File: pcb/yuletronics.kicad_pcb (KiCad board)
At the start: 2 copper layers, 45 x 50 mm, 35 parts, among them IC1 STM32F042F6P6, IC2 MCP1700, IC3 TLV61225, J1 BATT, J2 MICROUSB, P1 SWD_TC, SW1 BOOTLOAD, SW2 PWR_SWITCH

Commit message: Version 1
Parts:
- removed D1, D2, D4, D7, D8: LED, agg:0805-LED
- removed R10, R11, R5, R6, R8, R9: R, agg:0805
- added D10: LED_RABG, yule:CREE_RGB_LED, F.Cu at (95.8, 82.8)
- added D13: LED_RABG, yule:CREE_RGB_LED, F.Cu at (143.0, 102.9)
- added D14: LED_RABG, yule:CREE_RGB_LED, F.Cu at (131.8, 70.2)
- added J3: CONN_01x08, yule:Interboard, B.Cu at (117.0, 55.5)
- added R12: 510, agg:0805, F.Cu at (108.0, 70.0)
- added R15: 510, agg:0805, F.Cu at (108.0, 72.0)
- added R17: 510, agg:0805, F.Cu at (96.0, 101.0)
- added R18: 510, agg:0805, F.Cu at (132.0, 85.0)
- added R20: 510, agg:0805, F.Cu at (96.0, 103.0)
- added R21: 510, agg:0805, F.Cu at (132.0, 83.0)
- added R23: 510, agg:0805, F.Cu at (96.0, 105.0)
- added R24: 510, agg:0805, F.Cu at (132.0, 81.0)
- added R26: 510, agg:0805, F.Cu at (100.0, 81.0)
- added R29: 510, agg:0805, F.Cu at (100.0, 83.0)
- added R32: 510, agg:0805, F.Cu at (100.0, 85.0)
- added R35: 510, agg:0805, F.Cu at (138.0, 105.0)
- added R36: 510, agg:0805, F.Cu at (126.0, 72.0)
- added R38: 510, agg:0805, F.Cu at (138.0, 103.0)
- added R39: 510, agg:0805, F.Cu at (126.0, 70.0)
- added R41: 510, agg:0805, F.Cu at (138.0, 101.0)
- added R42: 510, agg:0805, F.Cu at (126.0, 68.0)
- added SW3: BUTTON, yule:MOM_SWITCH, B.Cu at (132.0, 94.9)
- added X1: Silk_art, yule:tree_silk_scaled, F.Cu at (117.0, 89.8)
- D3, D5, D6: value LED -> LED_RABG; footprint agg:0805-LED -> yule:CREE_RGB_LED
- R4: value R -> 10k
- R7: value R -> 510
- SW1: footprint agg:MOM_SWITCH -> yule:MOM_SWITCH; moved to B.Cu
- SW2: moved to B.Cu
- moved D5 55.7 mm to (91.2, 102.9), turned to 0 degrees
- moved SW1 33.2 mm to (102.0, 94.9), turned to 270 degrees
- moved C5 32.6 mm to (105.0, 119.6), turned to 180 degrees
- moved D3 32.2 mm to (102.2, 70.2), turned to 0 degrees
- moved R7 30.5 mm to (108.0, 68.0), turned to 0 degrees
- moved C6 30.0 mm to (105.0, 122.2), turned to 180 degrees
- moved IC2 27.1 mm to (109.0, 121.4), turned to 0 degrees
- moved L1 25.8 mm to (105.5, 114.7)
- moved C7 25.7 mm to (105.5, 109.4)
- moved C4 25.6 mm to (105.5, 117.5)
- moved IC3 25.5 mm to (105.5, 112.2)
- moved R4 25.0 mm to (138.0, 98.2), turned to 0 degrees
- moved SW2 24.7 mm to (105.4, 105.3), turned to 0 degrees
- moved R1 24.2 mm to (107.0, 97.2), turned to 90 degrees
- moved J1 13.9 mm to (117.0, 114.9), turned to 180 degrees
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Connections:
- D3 pad 1: GND -> Net-(D3-Pad1)
- D3 pad 2: Net-(D3-Pad2) -> 3v3
- D5 pad 1: GND -> Net-(D5-Pad1)
- D5 pad 2: Net-(D5-Pad2) -> 3v3
- D6 pad 1: GND -> Net-(D6-Pad1)
- D6 pad 2: Net-(D6-Pad2) -> 3v3
- IC1 pad 10: /LED5 -> /LED2G
- IC1 pad 12: /LED6 -> /LED2B
- IC1 pad 13: /LED7 -> /BUTTON
- IC1 pad 14: /LED8 -> (no net)
- IC1 pad 2: Net-(IC1-Pad2) -> (no net)
- IC1 pad 3: Net-(IC1-Pad3) -> (no net)
- IC1 pad 4: Net-(IC1-Pad4) -> (no net)
- IC1 pad 6: /LED1 -> /LED1R
- IC1 pad 7: /LED2 -> /LED1G
- IC1 pad 8: /LED3 -> /LED1B
- IC1 pad 9: /LED4 -> /LED2R
- J2 pad 4: Net-(J2-Pad4) -> (no net)
- J2 pad S: Net-(J2-PadS) -> (no net)
- P1 pad 3: Net-(P1-Pad3) -> (no net)
- P1 pad 6: Net-(P1-Pad6) -> (no net)
- R4 pad 1: /LED1 -> /BUTTON
- R4 pad 2: Net-(D1-Pad2) -> GND
- R7 pad 1: /LED4 -> Net-(D3-Pad1)
- R7 pad 2: Net-(D4-Pad2) -> /LED1R
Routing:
- net 3v3: track 63.9 -> 226.8 mm, vias 2 -> 14
- net /LED2G: track 0.00 -> 115.4 mm, vias 0 -> 7
- net /LED2R: track 0.00 -> 113.2 mm, vias 0 -> 7
- net /LED1R: track 0.00 -> 110.4 mm, vias 0 -> 5
- net /LED2B: track 0.00 -> 110.3 mm, vias 0 -> 6
- net /LED1G: track 0.00 -> 106.3 mm, vias 0 -> 5
- net /LED1B: track 0.00 -> 103.3 mm, vias 0 -> 3
- net /LED6: track 32.1 -> 0.00 mm
- net /LED4: track 32.1 -> 0.00 mm
- net /LED7: track 28.7 -> 0.00 mm
- net /LED3: track 28.7 -> 0.00 mm
- net /BUTTON: track 0.00 -> 28.7 mm, vias 0 -> 4
- net /LED5: track 26.9 -> 0.00 mm, vias 2 -> 0
- net /LED8: track 25.4 -> 0.00 mm
- net /LED2: track 25.4 -> 0.00 mm
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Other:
- board size 45 x 50 mm -> 70 x 70 mm
- board text added: "Bootload"
- board text added: "Power"

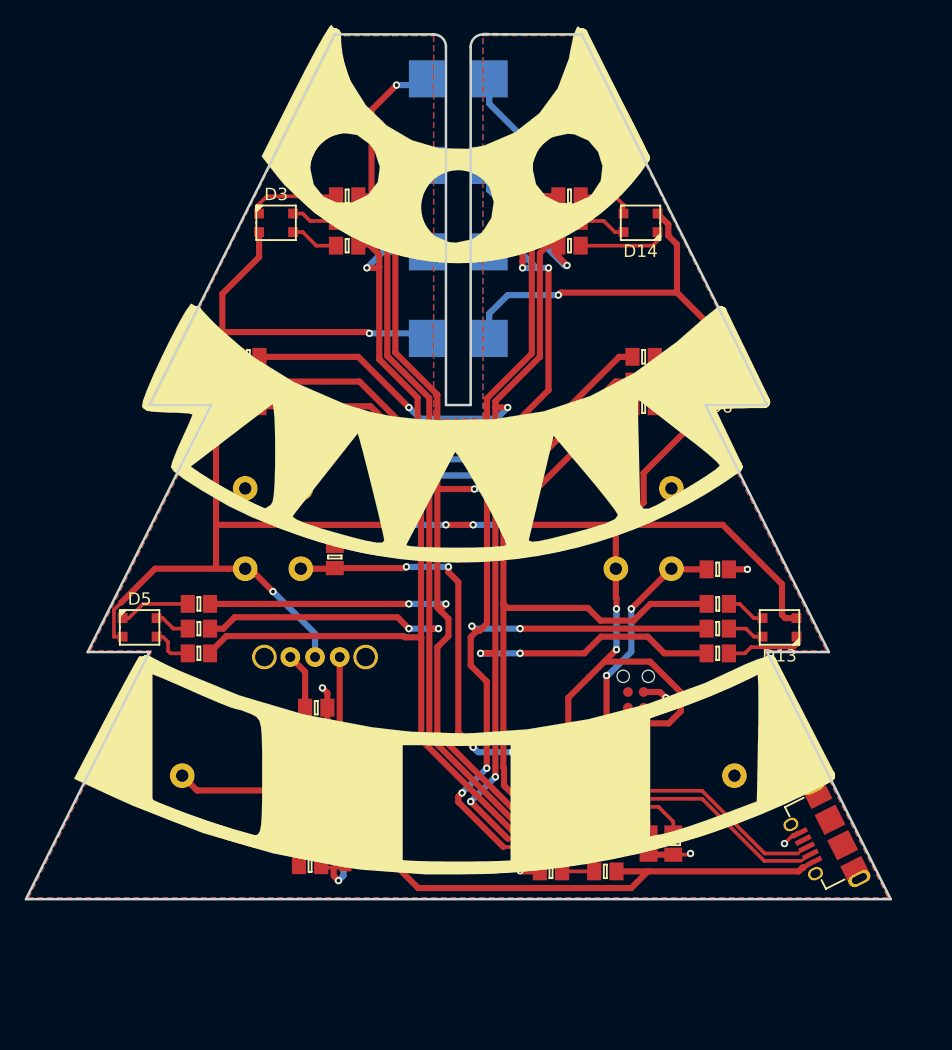
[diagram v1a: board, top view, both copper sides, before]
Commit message: Fix circuit to account for LED currents: change resistor values, upgrade LDO regulator, use transistor array
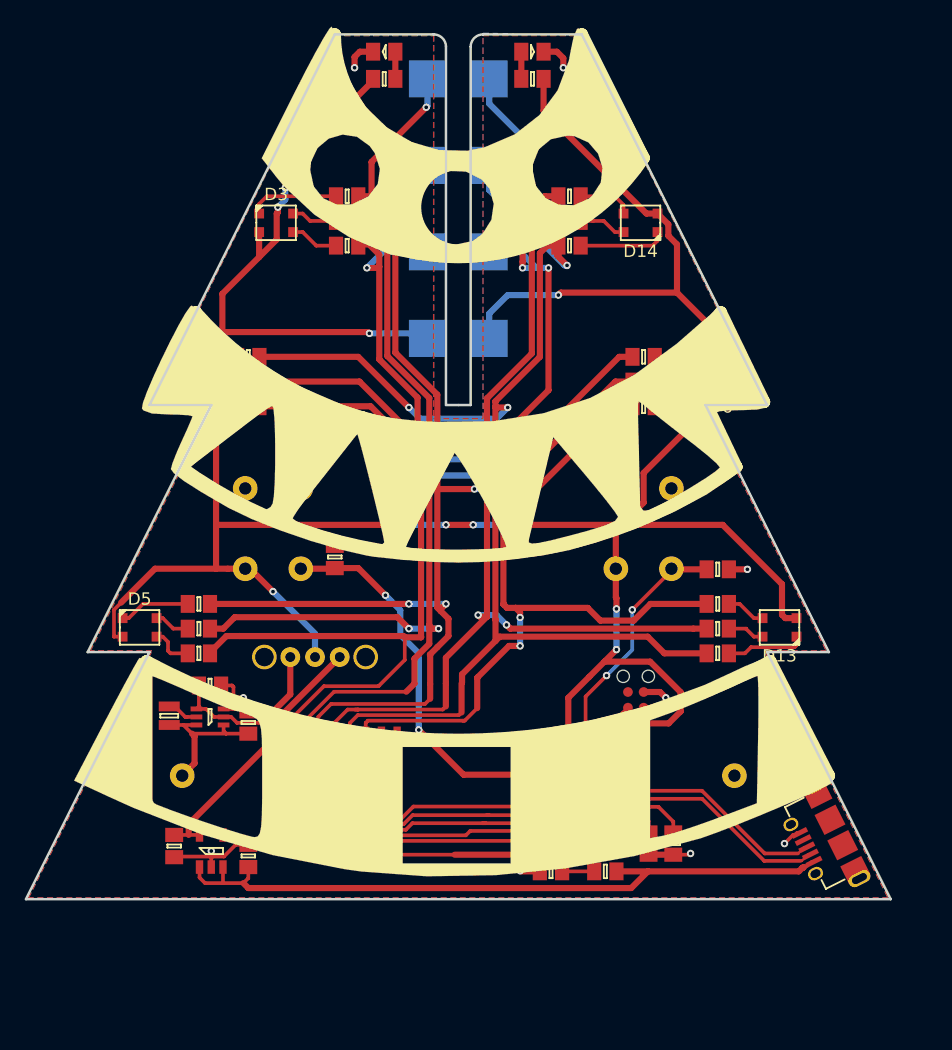
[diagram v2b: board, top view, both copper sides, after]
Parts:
- removed IC2: MCP1700, agg:SOT-23
- added D1: LED, agg:0805-LED, F.Cu at (111.0, 56.3)
- added D2: LED, agg:0805-LED, F.Cu at (123.0, 56.3)
- added R5: 100, agg:0805, F.Cu at (111.0, 58.5)
- added R6: 100, agg:0805, F.Cu at (123.0, 58.5)
- added U1: XC6210B332MR, agg:SOT-23-5, F.Cu at (97.0, 121.0)
- added U2: ULN2003D1013TR, agg:SOIC-16, F.Cu at (107.6, 114.4)
- R12, R15, R20, R21, R23, R24, R29, R32, R38, R39, R41, R42: value 510 -> 30
- R17, R18, R26, R35, R36, R7: value 510 -> 100
- SW3: value BUTTON -> BOOTLOAD
- moved L1 12.8 mm to (93.6, 110.0), turned to 90 degrees
- moved C6 11.1 mm to (94.0, 120.6), turned to 270 degrees
- moved IC3 8.83 mm to (96.9, 110.2)
- moved C4 8.82 mm to (100.0, 110.6), turned to 90 degrees
- moved C7 8.79 mm to (96.9, 107.6)
- moved C5 5.31 mm to (100.0, 121.4), turned to 90 degrees
- moved X1 0.15 mm to (117.0, 89.9)
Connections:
- IC1 pad 10: /LED2G -> /BUTTON
- IC1 pad 12: /LED2B -> /led_1B
- IC1 pad 13: /BUTTON -> /led_2B
- IC1 pad 6: /LED1R -> /led_2R
- IC1 pad 7: /LED1G -> /led_2G
- IC1 pad 8: /LED1B -> /led_1R
- IC1 pad 9: /LED2R -> /led_1G
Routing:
- net 3v3: track 226.8 -> 260.3 mm, vias 14 -> 16
- net /led_1B: track 0.00 -> 30.9 mm
- net /led_2B: track 0.00 -> 23.2 mm, vias 0 -> 2
- net /led_1G: track 0.00 -> 22.2 mm
- net /led_1R: track 0.00 -> 21.2 mm
- net /led_2G: track 0.00 -> 20.0 mm
- net /led_2R: track 0.00 -> 18.0 mm
- net 5v: track 45.7 -> 57.2 mm
- net /LED1B: track 103.3 -> 95.9 mm
- net /VBATT: track 19.5 -> 12.4 mm
- net /LED2R: track 113.2 -> 106.6 mm, vias 7 -> 3
- net GND: track 28.7 -> 34.9 mm, vias 10 -> 13
- net /LED2G: track 115.4 -> 109.2 mm, vias 7 -> 5
- net /LED2B: track 110.3 -> 105.5 mm
- net /LED1G: track 106.3 -> 101.9 mm
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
